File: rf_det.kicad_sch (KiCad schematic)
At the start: 18 parts, among them U2 AD8318, U3 AD8318

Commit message: MPN/PN update
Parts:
- C66: MPN (none) -> CL10B105KB8NQNC
- C67, C69, C72: MPN (none) -> C0603C104M5RAC7411
- C68, C70, C71, C73, C74: MPN (none) -> C0603C102J5GAC7411
- FB5: MPN (none) -> BLM18KG601SH1D
- R36, R38: MPN (none) -> CR0603-FX-52R3ELF; PN CR0603-FX-52R3ELF -> CR0603-FX-52R3ELF
- R37, R39: MPN (none) -> CRCW0603499RFKEA
- TP5: MPN (none) -> -
- U2, U3: MPN (none) -> AD8318ACPZ-REEL7
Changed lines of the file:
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@@
+      (effects (font (size 1.27 1.27)) hide)
+    )
+    (property "MPN" "BLM18KG601SH1D" (at 123.19 203.2 0)
       (effects (font (size 1.27 1.27)) hide)
     )
@@
       (effects (font (size 1.27 1.27)) hide)
     )
+    (property "MPN" "-" (at 135.89 133.35 0)
+      (effects (font (size 1.27 1.27)) hide)
+    )
     (pin "1")
     (instances
@@
     )
     (property "PN" " AD8318ACPZ-REEL7 " (at 110.49 101.6 0)
+      (effects (font (size 1.27 1.27)) hide)
+    )
+    (property "MPN" " AD8318ACPZ-REEL7 " (at 110.49 101.6 0)
       (effects (font (size 1.27 1.27)) hide)
     )
@@
       (effects (font (size 1.27 1.27)) hide)
     )
+    (property "MPN" "C0603C102J5GAC7411" (at 133.35 72.39 0)
+      (effects (font (size 1.27 1.27)) hide)
+    )
     (pin "1")
     (pin "2")
@@
       (effects (font (size 1.27 1.27)) hide)
     )
+    (property "MPN" "CRCW0603499RFKEA" (at 152.4 106.68 0)
+      (effects (font (size 1.27 1.27)) hide)
+    )
     (pin "1")
     (pin "2")
@@
       (effects (font (size 1.27 1.27)) hide)
     )
+    (property "MPN" "C0603C104M5RAC7411" (at 123.19 129.54 0)
+      (effects (font (size 1.27 1.27)) hide)
+    )
     (pin "1")
     (pin "2")
@@
     )
     (property "PN" " AD8318ACPZ-REEL7 " (at 275.59 101.6 0)
+      (effects (font (size 1.27 1.27)) hide)
+    )
+    (property "MPN" " AD8318ACPZ-REEL7 " (at 275.59 101.6 0)
       (effects (font (size 1.27 1.27)) hide)
     )
@@
       (effects (font (size 1.27 1.27)) hide)
     )
+    (property "MPN" "C0603C102J5GAC7411" (at 137.16 209.55 0)
+      (effects (font (size 1.27 1.27)) hide)
+    )
     (pin "1")
     (pin "2")
@@
     )
     (property "PN" "C0603C102J5GAC7411" (at 298.45 72.39 0)
+      (effects (font (size 1.27 1.27)) hide)
+    )
+    (property "MPN" "C0603C102J5GAC7411" (at 298.45 72.39 0)
       (effects (font (size 1.27 1.27)) hide)
     )
@@
       (effects (font (size 1.27 1.27)) hide)
     )
+    (property "MPN" "C0603C104M5RAC7411" (at 288.29 129.54 0)
+      (effects (font (size 1.27 1.27)) hide)
+    )
     (pin "1")
     (pin "2")
@@
       (effects (font (size 1.27 1.27)) hide)
     )
-    (property "PN" " CR0603-FX-52R3ELF " (at 294.64 67.31 0)
+    (property "PN" "CR0603-FX-52R3ELF" (at 294.64 67.31 0)
+      (effects (font (size 1.27 1.27)) hide)
+    )
+    (property "MPN" "CR0603-FX-52R3ELF" (at 294.64 67.31 0)
       (effects (font (size 1.27 1.27)) hide)
     )
@@
       (effects (font (size 1.27 1.27)) hide)
     )
-    (property "PN" " CR0603-FX-52R3ELF " (at 129.54 67.31 0)
+    (property "PN" "CR0603-FX-52R3ELF" (at 129.54 67.31 0)
+      (effects (font (size 1.27 1.27)) hide)
+    )
+    (property "MPN" "CR0603-FX-52R3ELF" (at 129.54 67.31 0)
       (effects (font (size 1.27 1.27)) hide)
     )
@@
       (effects (font (size 1.27 1.27)) hide)
     )
+    (property "MPN" "CRCW0603499RFKEA" (at 317.5 106.68 0)
+      (effects (font (size 1.27 1.27)) hide)
+    )
     (pin "1")
     (pin "2")
@@
     )
     (property "PN" "CL10B105KB8NQNC" (at 116.84 209.55 0)
+      (effects (font (size 1.27 1.27)) hide)
+    )
+    (property "MPN" "CL10B105KB8NQNC" (at 116.84 209.55 0)
       (effects (font (size 1.27 1.27)) hide)
     )
@@
       (effects (font (size 1.27 1.27)) hide)
     )
+    (property "MPN" "-" (at 300.99 133.35 0)
+      (effects (font (size 1.27 1.27)) hide)
+    )
     (pin "1")
     (instances
@@
       (effects (font (size 1.27 1.27)) hide)
     )
+    (property "MPN" "C0603C104M5RAC7411" (at 128.27 209.55 0)
+      (effects (font (size 1.27 1.27)) hide)
+    )
     (pin "1")
     (pin "2")
@@
       (effects (font (size 1.27 1.27)) hide)
     )
+    (property "MPN" "C0603C102J5GAC7411" (at 290.83 72.39 0)
+      (effects (font (size 1.27 1.27)) hide)
+    )
     (pin "1")
     (pin "2")
@@
       (effects (font (size 1.27 1.27)) hide)
     )
+    (property "MPN" "C0603C102J5GAC7411" (at 125.73 72.39 0)
+      (effects (font (size 1.27 1.27)) hide)
+    )

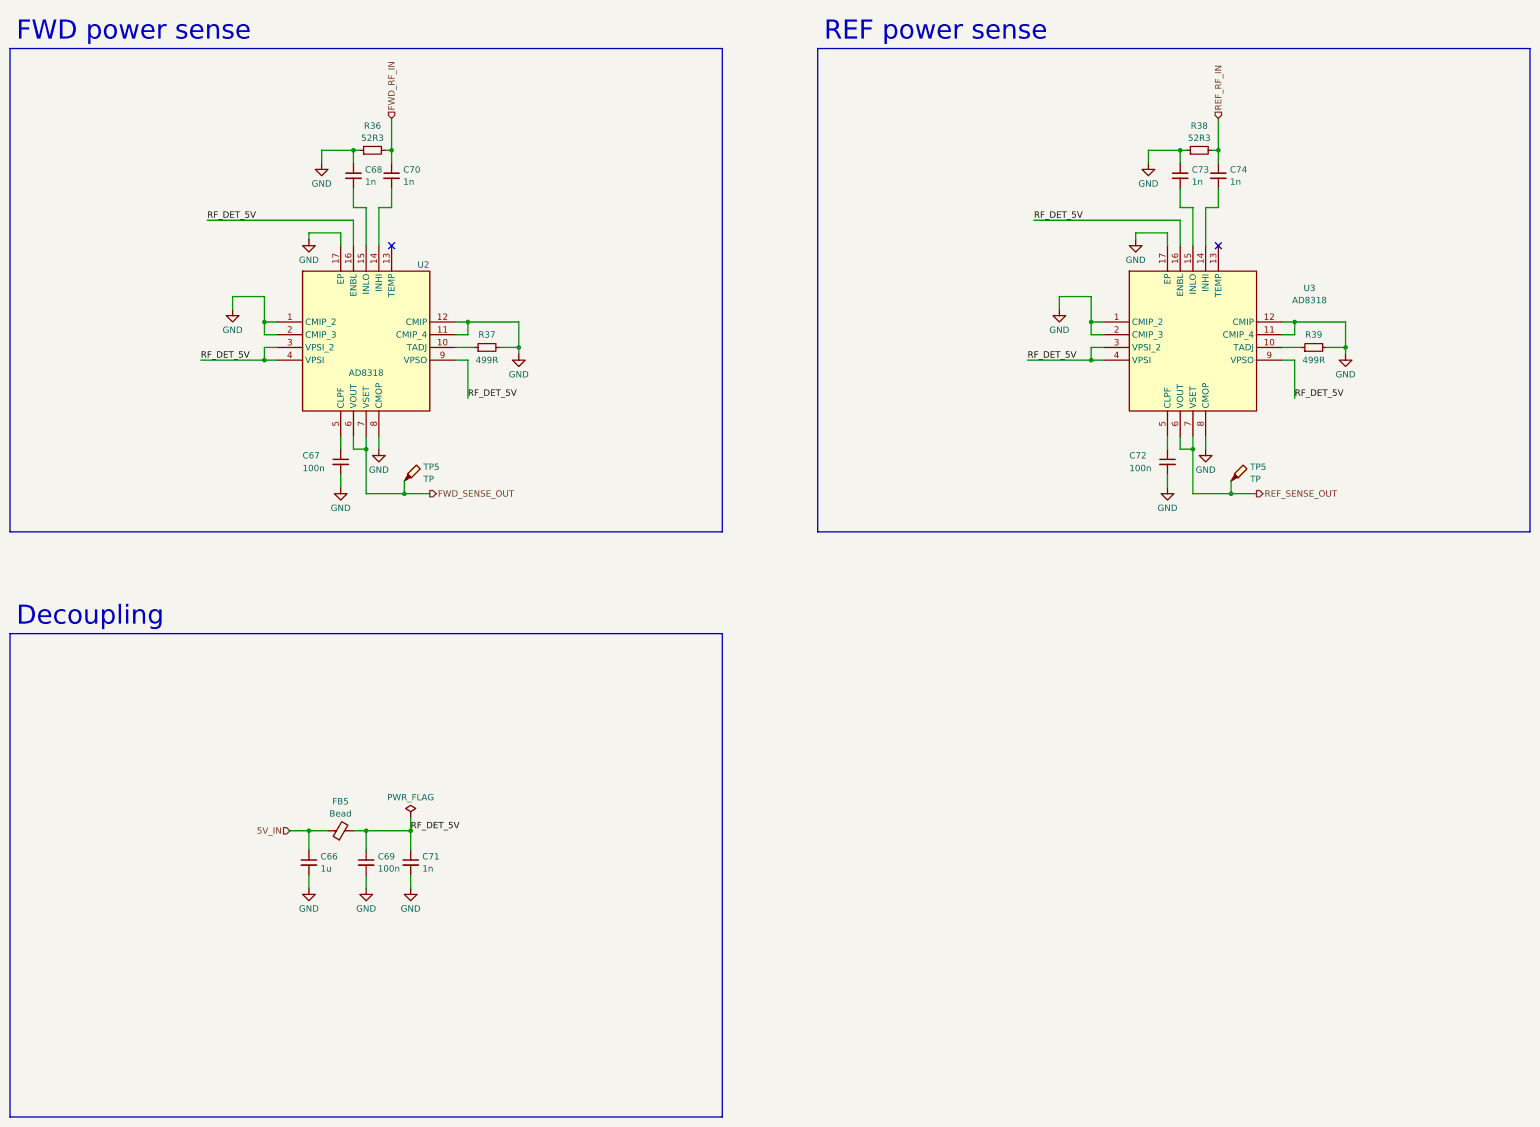
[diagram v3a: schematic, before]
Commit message: WIP rev B
- replaced R44-R46 with 22k
- exposed BOOT0 at the DA15 connector
- added a testpoint at DAC OUT2
- added a buffer to the 40MHz reference oscillator
- removed C2
- bypassed R5 with a 100nF capacitor
- changed D5's voltage to 5.1V
- routed TX_SAMP_CLK
- changed temperature sensor's supply voltage to 5V
- added a series of 100p, 1n and 10n capacitors at PA_VGG
- reduced N-connector cutouts to 2.5mm
- improved RF output track a little
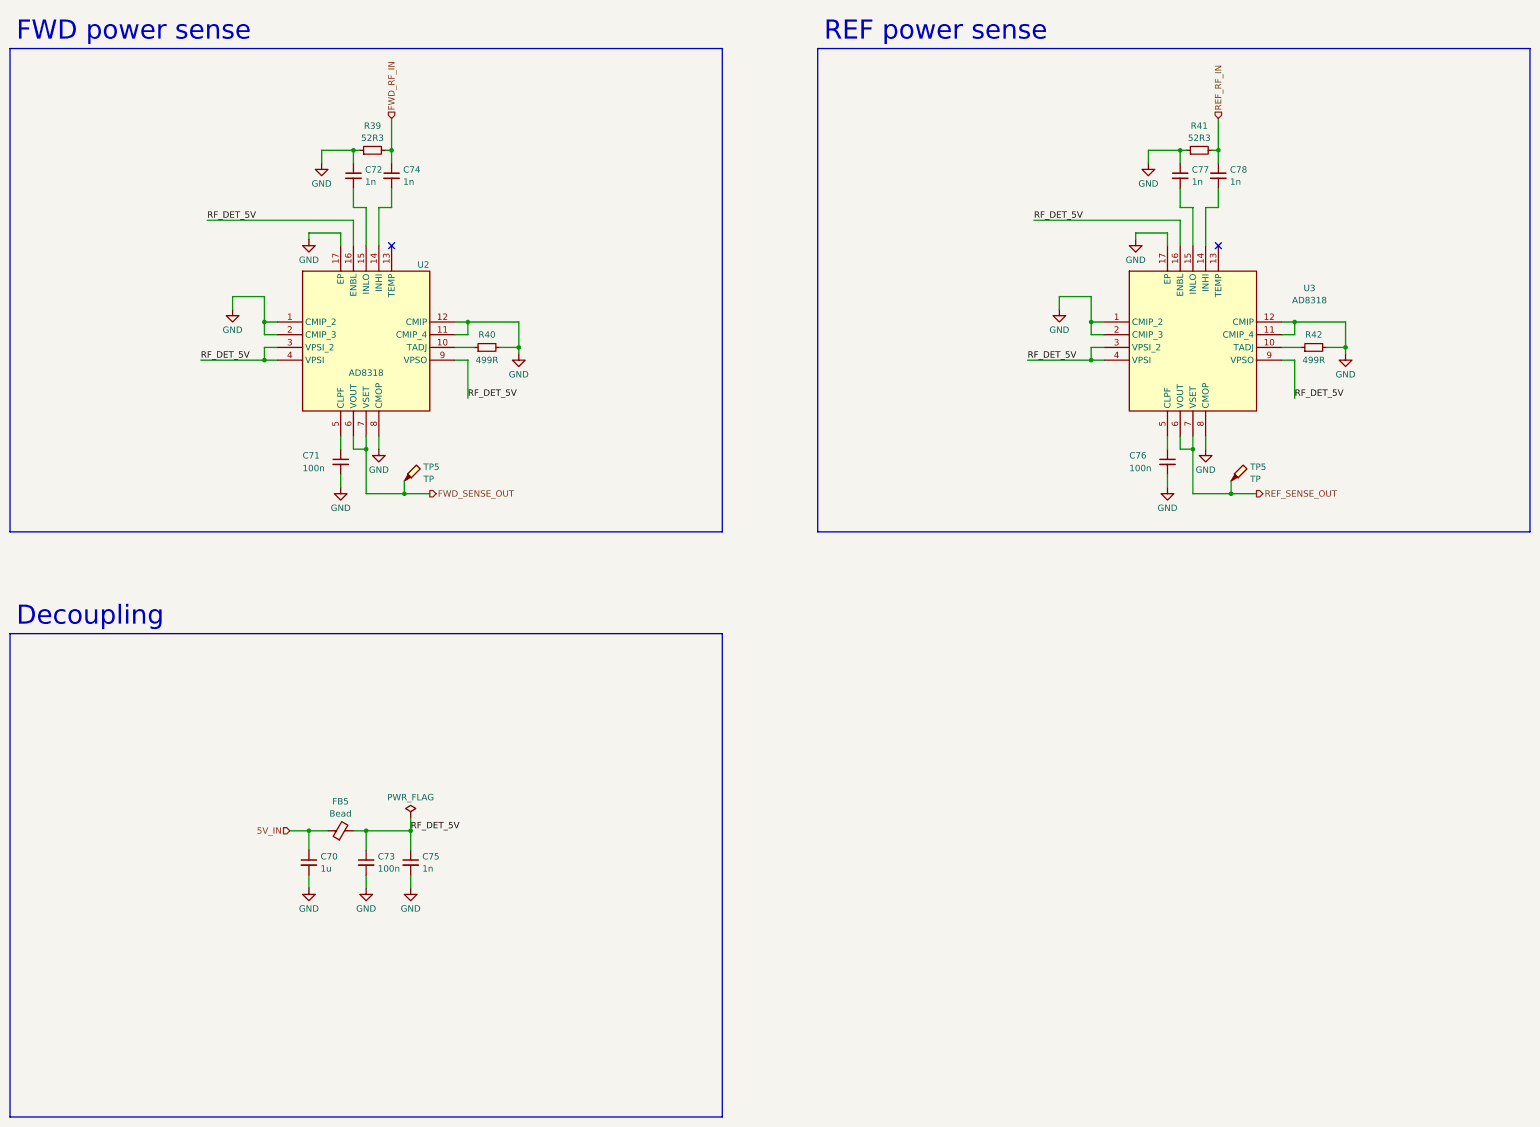
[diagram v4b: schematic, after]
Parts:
- renumbered C66 to C70, C67 to C71, C68 to C72, C69 to C73, C70 to C74, C71 to C75, C72 to C76, C73 to C77, C74 to C78, R36 to R39, R37 to R40, R38 to R41, R39 to R42

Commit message: WIP rev B
- added bleed resistors
- power supply now uses linear regulators
- routed RX_SAMP_CLK
- added some decoupling at RF_PA_VDD
- added some GND vias here and there
- updated BOM
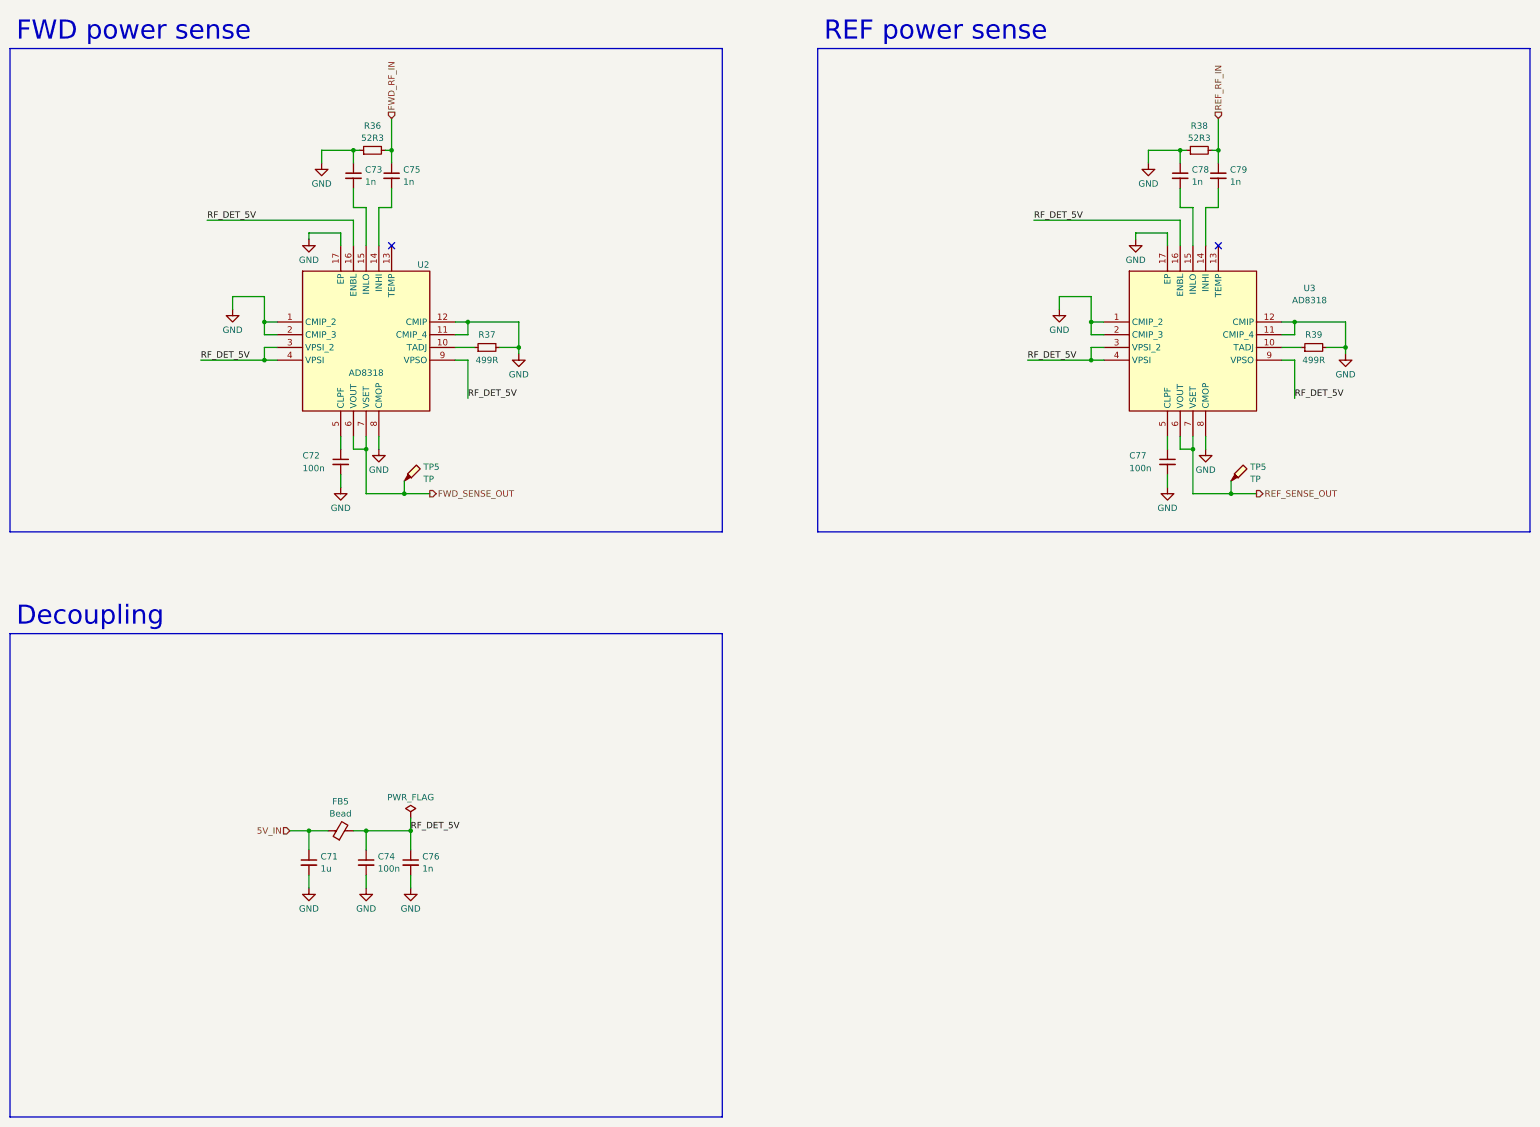
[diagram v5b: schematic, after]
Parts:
- renumbered C70 to C71, C71 to C72, C72 to C73, C73 to C74, C74 to C75, C75 to C76, C76 to C77, C77 to C78, C78 to C79, R39 to R36, R40 to R37, R41 to R38, R42 to R39

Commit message: minor changes
footprint name change
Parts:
- U2, U3: footprint QFN65P400X400X100-17N -> Mine:QFN65P400X400X100-17N
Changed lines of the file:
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@@
       (effects (font (size 1.27 1.27)))
     )
-    (property "Footprint" "QFN65P400X400X100-17N" (at 142.24 188.9 0)
+    (property "Footprint" "Mine:QFN65P400X400X100-17N" (at 142.24 188.9 0)
       (effects (font (size 1.27 1.27)) (justify left top) hide)
     )
@@
       (effects (font (size 1.27 1.27)))
     )
-    (property "Footprint" "QFN65P400X400X100-17N" (at 307.34 188.9 0)
-      (effects (font (size 1.27 1.27)) (justify left top) hide)
-    )
+    (property "Footprint" "Mine:QFN65P400X400X100-17N" (at 307.34 188.9 0)
+      (effects (font (size 1.27 1.27)) (justify left top) hide)
+    )

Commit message: removed extra space
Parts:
- U2, U3: MPN AD8318ACPZ-REEL7 -> AD8318ACPZ-REEL7; PN AD8318ACPZ-REEL7 -> AD8318ACPZ-REEL7
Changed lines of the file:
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@@
       (effects (font (size 1.27 1.27)) (justify left top) hide)
     )
-    (property "PN" " AD8318ACPZ-REEL7 " (at 110.49 101.6 0)
-      (effects (font (size 1.27 1.27)) hide)
-    )
-    (property "MPN" " AD8318ACPZ-REEL7 " (at 110.49 101.6 0)
+    (property "PN" "AD8318ACPZ-REEL7 " (at 110.49 101.6 0)
+      (effects (font (size 1.27 1.27)) hide)
+    )
+    (property "MPN" "AD8318ACPZ-REEL7 " (at 110.49 101.6 0)
       (effects (font (size 1.27 1.27)) hide)
     )
@@
       (effects (font (size 1.27 1.27)) (justify left top) hide)
     )
-    (property "PN" " AD8318ACPZ-REEL7 " (at 275.59 101.6 0)
-      (effects (font (size 1.27 1.27)) hide)
-    )
-    (property "MPN" " AD8318ACPZ-REEL7 " (at 275.59 101.6 0)
-      (effects (font (size 1.27 1.27)) hide)
-    )
+    (property "PN" "AD8318ACPZ-REEL7 " (at 275.59 101.6 0)
+      (effects (font (size 1.27 1.27)) hide)
+    )
+    (property "MPN" "AD8318ACPZ-REEL7 " (at 275.59 101.6 0)
+      (effects (font (size 1.27 1.27)) hide)
+    )
